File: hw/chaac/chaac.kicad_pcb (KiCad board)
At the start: 2 copper layers, 85 x 65 mm, 78 parts, among them J1 windrain, J10 Solar Panel, J11 FAN, J12 GPS, J2 Conn_01x02, J3 UART, J4 Battery, J5 Power, J6 Light, J7 AM2315, J8 TC2030-CTX, J9 Therm, SW1 RST, U1 MIC550X, U2 STM32L432, U3 XBEE_S2C, U5 BMP280, U6 MCP73871, U7 XCL102, Y1 32.768kHz

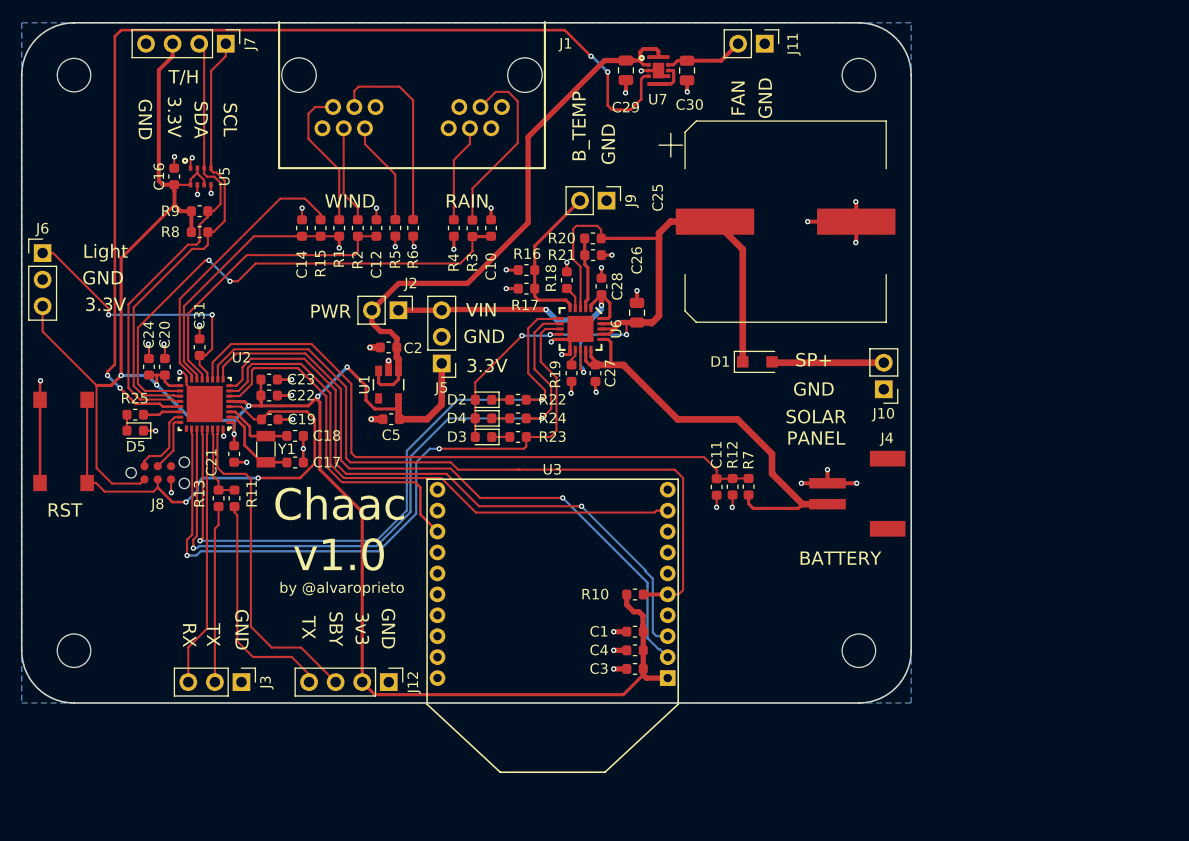
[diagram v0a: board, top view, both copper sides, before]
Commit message: Updated Chaac HW to v1.1
Added gate for controlling power to wind direction sensor and light sensor.
(This should allow for power gating for lower power consumption)

Removed all GPS stuff (won't be using it this time)

Removed fan driver. (also won't be using it)

Added pull down resistors on xbee enable and boot0.

Fixed battery charger bug (PROG1 and PROG2 were flipped)
Added 1k resistor to therm pin

Flipped wind/rain connector location for simpler routing
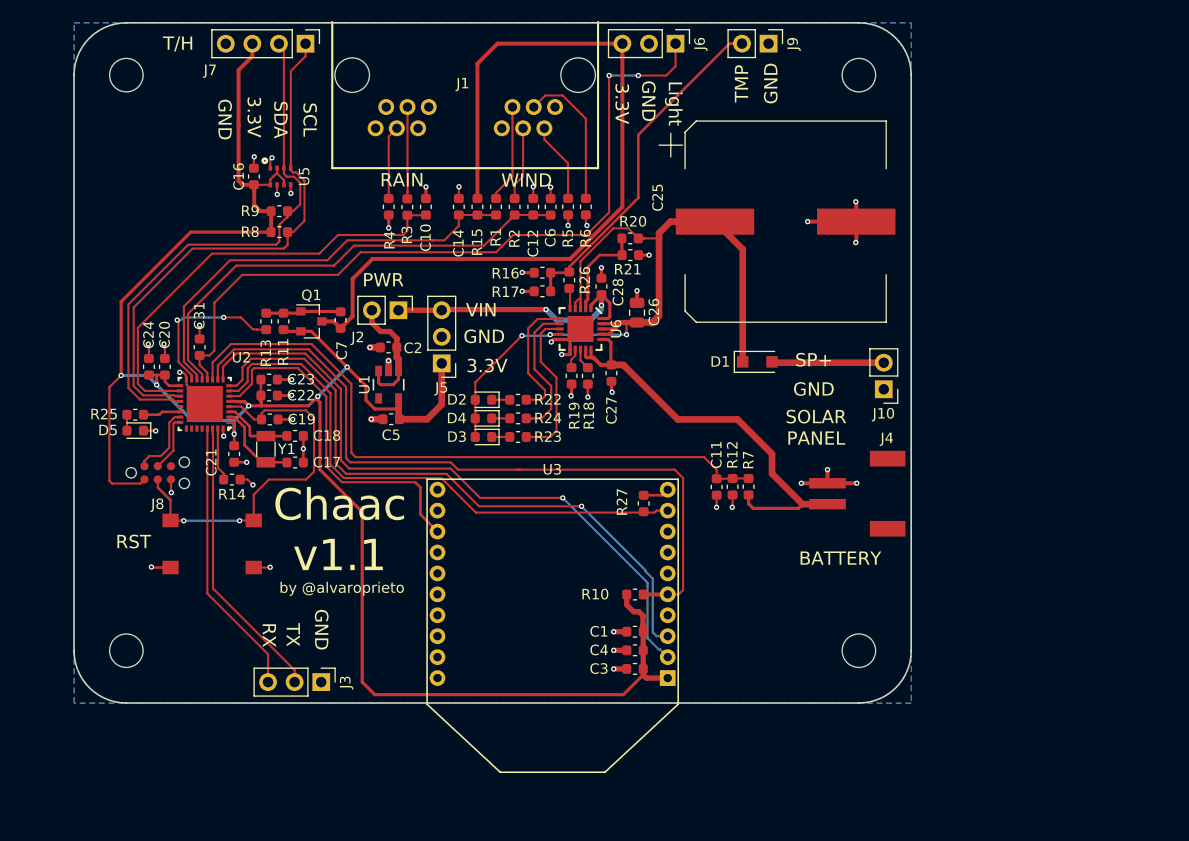
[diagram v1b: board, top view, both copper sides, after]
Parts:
- removed C29, C30: 10uF, Capacitor_SMD:C_0805_2012Metric
- removed J11: FAN, Connector_PinHeader_2.54mm:PinHeader_1x02_P2.54mm_Vertical
- removed J12: GPS, Connector_PinHeader_2.54mm:PinHeader_1x04_P2.54mm_Vertical
- removed U7: XCL102, alvarop:XCL102
- added C6: 0.01 uF, Capacitor_SMD:C_0603_1608Metric, F.Cu at (145.5, 62.6)
- added C7: DNP, Capacitor_SMD:C_0603_1608Metric, F.Cu at (125.5, 73.4)
- added Q1: Q_PMOS_GSD, Package_TO_SOT_SMD:SOT-23, F.Cu at (122.7, 73.5)
- added R14: 10k, Resistor_SMD:R_0603_1608Metric, F.Cu at (115.1, 88.6)
- added R26: 1k, Resistor_SMD:R_0603_1608Metric, F.Cu at (147.3, 69.6)
- added R27: 10k, Resistor_SMD:R_0603_1608Metric, F.Cu at (154.4, 90.9)
- C10, C14: value 0.01 uF -> 0.1uF
- R11: value 0 -> 10k
- moved J6 63.7 mm to (157.5, 47.0), turned to 270 degrees
- moved J9 21.6 mm to (166.4, 47.0)
- moved R11 17.5 mm to (120.0, 73.5)
- moved R13 17.5 mm to (118.4, 73.5), turned to 90 degrees
- moved SW1 17.2 mm to (113.2, 94.8), turned to 180 degrees
- moved R5 16.6 mm to (147.2, 62.6)
- moved R6 16.6 mm to (148.9, 62.6)
- moved C12 15.1 mm to (143.9, 62.6)
- moved R2 15.1 mm to (142.1, 62.6)
- moved C14 15.1 mm to (136.8, 62.6)
- moved R15 15.1 mm to (138.5, 62.6)
- moved R1 15.1 mm to (140.3, 62.6)
- moved R18 9.37 mm to (149.1, 78.7), turned to 90 degrees
- moved C16 7.62 mm to (117.2, 59.7)
- moved J3 7.62 mm to (123.6, 108.0)
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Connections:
- C10 pad 1: /RAIN -> GND
- C10 pad 2: GND -> /RAIN
- J3 pad 2: Net-(J3-Pad2) -> /UART_RX
- J6 pad 3: +3V3 -> /SNS_3V3
- R1 pad 1: Net-(J1-Pad11) -> Net-(J1-Pad5)
- R11 pad 1: /UART_RX -> Net-(C7-Pad2)
- R11 pad 2: /GPS_TX -> +3V3
- R13 pad 1: /UART_RX -> /SNS_3V3_EN
- R13 pad 2: Net-(J3-Pad2) -> Net-(C7-Pad2)
- R15 pad 2: /WDIR_EN -> /SNS_3V3
- R2 pad 2: Net-(J1-Pad10) -> Net-(J1-Pad4)
- R22 pad 1: /nPG -> Net-(R22-Pad1)
- R23 pad 1: /STAT1 -> Net-(R23-Pad1)
- R24 pad 1: /STAT2 -> Net-(R24-Pad1)
- R3 pad 2: Net-(J1-Pad3) -> Net-(J1-Pad9)
- R4 pad 1: Net-(J1-Pad4) -> Net-(J1-Pad10)
- R5 pad 2: Net-(J1-Pad8) -> Net-(J1-Pad2)
- R6 pad 2: Net-(J1-Pad9) -> Net-(J1-Pad3)
- U2 pad 15: /WDIR_EN -> /SNS_3V3_EN
- U2 pad 21: /FAN_EN -> Net-(U2-Pad21)
- U2 pad 26: /STAT1 -> Net-(U2-Pad26)
- U2 pad 27: /STAT2 -> Net-(U2-Pad27)
- U2 pad 28: /nPG -> Net-(U2-Pad28)
- U2 pad 31: /GPS_SBY -> Net-(R14-Pad2)
- U6 pad 13: /MCP_VIN -> Net-(R18-Pad2)
- U6 pad 4: Net-(R18-Pad2) -> /MCP_VIN
- U6 pad 5: Net-(J9-Pad2) -> Net-(R26-Pad1)
- U6 pad 6: /nPG -> Net-(R22-Pad1)
- U6 pad 7: /STAT2 -> Net-(R24-Pad1)
- U6 pad 8: /STAT1 -> Net-(R23-Pad1)
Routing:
- net /FAN_EN: track 99.6 -> 0.00 mm, vias 4 -> 0
- net /SNS_3V3: track 0.00 -> 79.0 mm
- net /STAT1: track 67.9 -> 0.00 mm, vias 2 -> 0
- net /STAT2: track 66.6 -> 0.00 mm, vias 2 -> 0
- net /nPG: track 64.9 -> 0.00 mm, vias 2 -> 0
- net /LIGHT: track 26.3 -> 72.0 mm
- net Net-(C2-Pad1): track 56.3 -> 11.6 mm
- net /GPS_SBY: track 31.8 -> 0.00 mm
- net /WDIR_EN: track 26.7 -> 0.00 mm
- net /GPS_TX: track 21.9 -> 0.00 mm
- net /UART_RX: track 7.63 -> 27.5 mm
- net Net-(J9-Pad2): track 15.0 -> 32.9 mm
- net Net-(J3-Pad2): track 16.9 -> 0.00 mm
- net /WSPEED: track 28.8 -> 45.4 mm
- net /WDIR: track 26.2 -> 41.7 mm, vias 1 -> 0
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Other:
- board size 85 x 65 mm -> 80 x 65 mm
- board text added: "Chaac v1.1"
- board text added: "TMP"
- board text removed: "3v3"
- board text removed: "B_TEMP"
- board text removed: "Chaac v1.0"
- board text removed: "FAN"
- board text removed: "SBY"

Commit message: Did layout/schematic for chaac v1.2
Added extra led, boot button, and sense resistors for solar panel voltage
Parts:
- removed J2: Conn_01x02, Connector_PinHeader_2.54mm:PinHeader_1x02_P2.54mm_Vertical
- added C8: 0.1uF, Capacitor_SMD:C_0603_1608Metric, F.Cu at (107.9, 74.4)
- added D6: LED_ALT, LED_SMD:LED_0603_1608Metric, F.Cu at (111.5, 99.0)
- added R28: 100k, Resistor_SMD:R_0603_1608Metric, F.Cu at (166.0, 79.5)
- added R29: 100k, Resistor_SMD:R_0603_1608Metric, F.Cu at (166.0, 81.1)
- added R30: 10k, Resistor_SMD:R_0603_1608Metric, F.Cu at (111.5, 96.0)
- added SW2: RST, alvarop:PTS645SM43SMTR92, F.Cu at (103.9, 59.2)
- moved C11 48.6 mm to (115.1, 74.7), turned to 180 degrees
- moved SW1 35.7 mm to (110.2, 59.2), turned to 90 degrees
- moved J10 17.8 mm to (177.4, 97.8)
- moved D5 15.6 mm to (109.7, 99.1), turned to 90 degrees
- moved R25 14.1 mm to (109.7, 96.0), turned to 90 degrees
- moved J4 13.5 mm to (165.3, 101.8), turned to 180 degrees
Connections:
- C2 pad 1: Net-(C2-Pad1) -> /VIN
- U1 pad 1: Net-(C2-Pad1) -> /VIN
- U1 pad 3: Net-(C2-Pad1) -> /VIN
- U2 pad 15: /SNS_3V3_EN -> /VSOLAR
- U2 pad 26: Net-(U2-Pad26) -> /SNS_3V3_EN
- U2 pad 27: Net-(U2-Pad27) -> /BOOT
- U2 pad 28: Net-(U2-Pad28) -> /LED2
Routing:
- net /VSOLAR: track 0.00 -> 89.7 mm, vias 0 -> 8
- net /BOOT: track 0.00 -> 57.4 mm
- net /nRST: track 36.2 -> 85.0 mm, vias 2 -> 3
- net /SNS_3V3_EN: track 15.3 -> 51.9 mm
- net /LED1: track 3.62 -> 22.9 mm, vias 0 -> 2
- net /SOLAR_IN: track 10.7 -> 26.8 mm
- net /LED2: track 0.00 -> 11.8 mm
- net Net-(C2-Pad1): track 11.6 -> 0.00 mm
- net /VIN: track 26.7 -> 36.1 mm
- net GND: track 77.3 -> 84.4 mm, vias 50 -> 52
- net /UART_RX: track 27.5 -> 31.3 mm
- net /VBATT: track 41.3 -> 45.1 mm
- net Net-(D6-Pad2): track 0.00 -> 1.47 mm
- net /UART_TX: track 26.6 -> 28.0 mm
- net /BATT: track 63.3 -> 64.3 mm
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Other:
- board text added: "BOOT"
- board text added: "Chaac v1.2"
- board text removed: "Chaac v1.1"

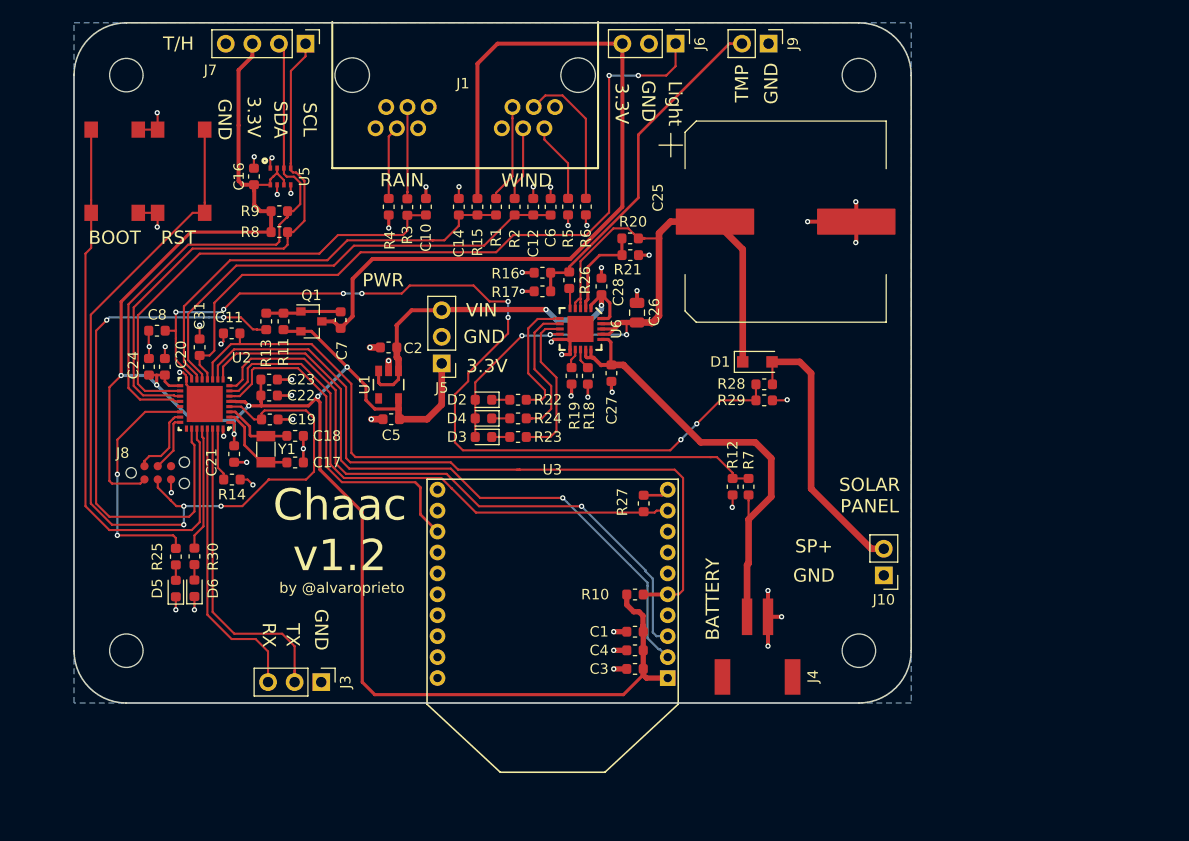
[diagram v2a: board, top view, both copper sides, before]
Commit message: Released chaac v2.0 to JLCPCB
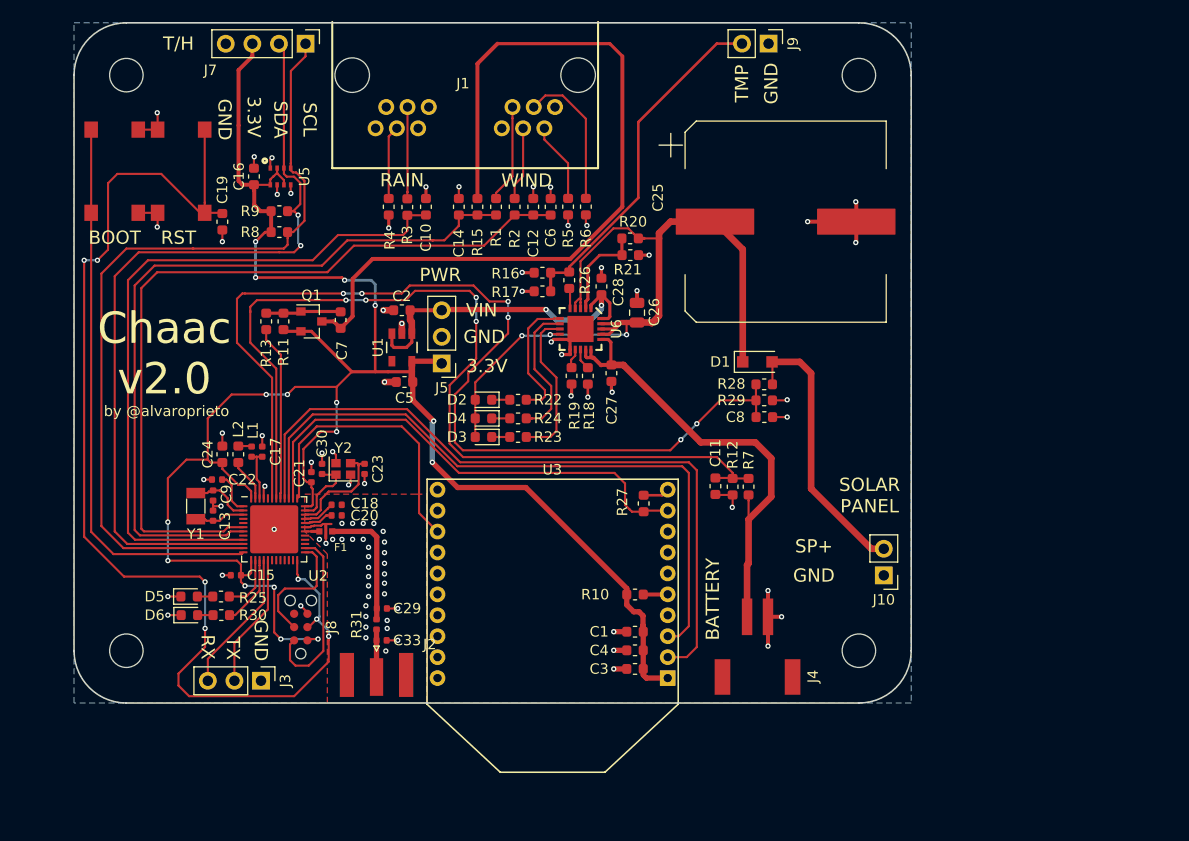
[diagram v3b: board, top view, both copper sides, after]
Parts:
- removed C31: 0.1uF, Capacitor_SMD:C_0603_1608Metric
- removed J6: Light, Connector_PinHeader_2.54mm:PinHeader_1x03_P2.54mm_Vertical
- removed R14: 10k, Resistor_SMD:R_0603_1608Metric
- added C13: 12pF, Capacitor_SMD:C_0402_1005Metric, F.Cu at (113.3, 92.1)
- added C15: 0.1uF, Capacitor_SMD:C_0402_1005Metric, F.Cu at (115.5, 97.8)
- added C29: DNP, Capacitor_SMD:C_0402_1005Metric, F.Cu at (129.4, 101.0)
- added C30: 12pF, Capacitor_SMD:C_0402_1005Metric, F.Cu at (123.7, 87.6)
- added C33: DNP, Capacitor_SMD:C_0402_1005Metric, F.Cu at (129.4, 104.0)
- added C9: 12pF, Capacitor_SMD:C_0402_1005Metric, F.Cu at (113.3, 90.2)
- added F1: 2450FM07A0029T, alvarop:2450FM07A0029T, F.Cu at (124.1, 93.6)
- added J2: RP_SMA, Connector_Coaxial:SMA_Samtec_SMA-J-P-H-ST-EM1_EdgeMount, F.Cu at (128.9, 107.3)
- added L1: 15nH, Inductor_SMD:L_0402_1005Metric, F.Cu at (117.0, 86.0)
- added L2: 10uH, Inductor_SMD:L_0603_1608Metric, F.Cu at (115.7, 86.2)
- added R31: 0, Resistor_SMD:R_0402_1005Metric, F.Cu at (128.9, 102.5)
- added Y2: 32MHz, Crystal:Crystal_SMD_2016-4Pin_2.0x1.6mm, F.Cu at (125.7, 87.6)
- C17: value 6pF -> 1uF; footprint Capacitor_SMD:C_0603_1608Metric -> Capacitor_SMD:C_0402_1005Metric
- C18: value 6pF -> 100pF; footprint Capacitor_SMD:C_0603_1608Metric -> Capacitor_SMD:C_0402_1005Metric
- C20: value 0.1uF -> DNP; footprint Capacitor_SMD:C_0603_1608Metric -> Capacitor_SMD:C_0402_1005Metric
- C21: footprint Capacitor_SMD:C_0603_1608Metric -> Capacitor_SMD:C_0402_1005Metric
- C22: value 0.01 uF -> 0.1uF; footprint Capacitor_SMD:C_0603_1608Metric -> Capacitor_SMD:C_0402_1005Metric
- C23: value 0.1uF -> 12pF; footprint Capacitor_SMD:C_0603_1608Metric -> Capacitor_SMD:C_0402_1005Metric
- U2: value STM32L432 -> NRF52811-QFAA; footprint alvarop:UFQFPN32 -> Package_DFN_QFN:QFN-48-1EP_6x6mm_P0.4mm_EP4.6x4.6mm
- moved C8 58.6 mm to (166.0, 82.7), turned to 0 degrees
- moved C11 48.5 mm to (161.3, 89.3), turned to 270 degrees
- moved C20 21.7 mm to (125.1, 92.1), turned to 180 degrees
- moved J8 20.1 mm to (121.7, 102.7), turned to 90 degrees
- moved C19 19.4 mm to (114.2, 64.0), turned to 270 degrees
- moved U2 13.7 mm to (119.1, 93.4), turned to 0 degrees
- moved C23 12.5 mm to (127.8, 87.6), turned to 90 degrees
- moved C24 10.9 mm to (114.2, 86.2)
- moved C22 9.45 mm to (113.7, 88.6), turned to 180 degrees
- moved Y1 8.63 mm to (111.6, 91.2), turned to 90 degrees
- moved C21 7.71 mm to (122.7, 88.4), turned to 90 degrees
- moved C18 7.69 mm to (125.1, 91.1), turned to 180 degrees
- moved R30 6.17 mm to (114.1, 101.6), turned to 0 degrees
- moved R25 5.76 mm to (114.0, 99.8), turned to 0 degrees
- moved J3 5.76 mm to (117.9, 107.9)
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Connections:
- C18 pad 1: Net-(C18-Pad1) -> GND
- C18 pad 2: GND -> Net-(C18-Pad2)
- C20 pad 1: +3V3 -> GND
- C20 pad 2: GND -> Net-(C20-Pad2)
- C22 pad 1: +3V3 -> Net-(C22-Pad1)
- C23 pad 1: +3V3 -> GND
- C23 pad 2: GND -> Net-(C23-Pad2)
- R10 pad 1: /XB_nRST -> Net-(R10-Pad1)
- U2 pad 1: +3V3 -> Net-(C22-Pad1)
- U2 pad 10: /XB_nRST -> /SDA
- U2 pad 11: /BATT -> /SCL
- U2 pad 12: /LIGHT -> /BOOT
- U2 pad 13: /WSPEED -> +3V3
- U2 pad 14: /WDIR -> /LED1
- U2 pad 15: /VSOLAR -> /LED2
- U2 pad 16: GND -> /UART_TX
- U2 pad 17: +3V3 -> /UART_RX
- U2 pad 18: /RAIN -> Net-(U2-Pad18)
- U2 pad 19: /SCL -> Net-(U2-Pad19)
- U2 pad 2: Net-(C17-Pad1) -> Net-(C9-Pad1)
- U2 pad 20: /SDA -> Net-(U2-Pad20)
- U2 pad 22: /LED1 -> Net-(U2-Pad22)
- U2 pad 23: /SWDIO -> Net-(U2-Pad23)
- U2 pad 24: /SWCLK -> /nRST
- U2 pad 25: Net-(U2-Pad25) -> /SWCLK
- U2 pad 26: /SNS_3V3_EN -> /SWDIO
- U2 pad 27: /BOOT -> Net-(U2-Pad27)
- U2 pad 28: /LED2 -> Net-(U2-Pad28)
- U2 pad 29: /UART_TX -> Net-(U2-Pad29)
- U2 pad 3: Net-(C18-Pad1) -> Net-(C13-Pad1)
- U2 pad 30: /UART_RX -> Net-(F1-Pad1)
- U2 pad 31: Net-(R14-Pad2) -> GND
- U2 pad 32: GND -> Net-(C20-Pad2)
- U2 pad 4: /nRST -> Net-(U2-Pad4)
- U2 pad 5: +3V3 -> Net-(U2-Pad5)
- U2 pad 6: /XB_ON -> /WSPEED
- U2 pad 7: /XB_nSBY -> /WDIR
- U2 pad 8: /XB_RX -> Net-(U2-Pad8)
- U2 pad 9: /XB_TX -> /RAIN
- U3 pad 5: /XB_nRST -> Net-(R10-Pad1)
- Y1 pad 1: Net-(C17-Pad1) -> Net-(C9-Pad1)
- Y1 pad 2: Net-(C18-Pad1) -> Net-(C13-Pad1)
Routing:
- net /LIGHT: track 72.0 -> 0.00 mm, vias 2 -> 0
- net /XB_nRST: track 70.5 -> 0.00 mm
- net /SNS_3V3_EN: track 51.9 -> 16.7 mm, vias 2 -> 0
- net /WDIR: track 41.7 -> 72.2 mm
- net /WSPEED: track 45.4 -> 75.0 mm
- net /SCL: track 51.0 -> 79.1 mm
- net /SDA: track 51.7 -> 78.4 mm, vias 0 -> 2
- net /BATT: track 64.3 -> 89.1 mm, vias 0 -> 4
- net /nRST: track 85.0 -> 109.6 mm, vias 3 -> 7
- net /RAIN: track 43.2 -> 67.3 mm
- net /UART_RX: track 31.3 -> 12.8 mm
- net /LED1: track 22.9 -> 5.46 mm, vias 2 -> 0
- net /UART_TX: track 28.0 -> 13.7 mm
- net Net-(C29-Pad1): track 0.00 -> 12.4 mm
- net Net-(C23-Pad2): track 0.00 -> 10.3 mm
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- added copper zone on F.Cu, net GND
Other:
- board text added: "Chaac v2.0"
- board text removed: "Chaac v1.2"
- board text removed: "Light"
